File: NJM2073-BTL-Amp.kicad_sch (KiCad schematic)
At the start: 80 parts, among them J1 Screw_Terminal_01x02, J2 Screw_Terminal_01x02, J3 Barrel_Jack_Switch, J4 Conn_Coaxial_x2, J5 AudioJack3_SwitchTR, U3 NJM4558, U4 NJM4558

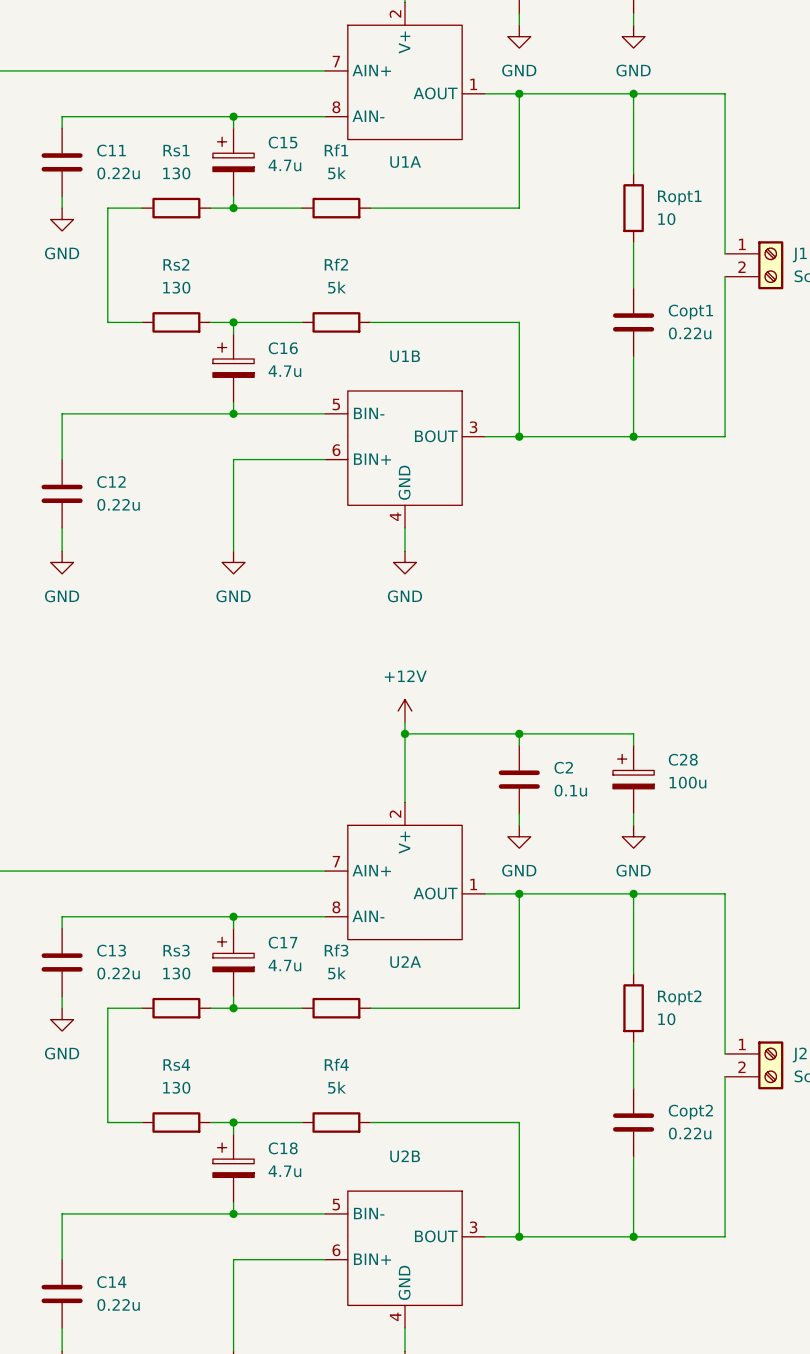
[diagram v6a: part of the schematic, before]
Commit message: シンボル名修正
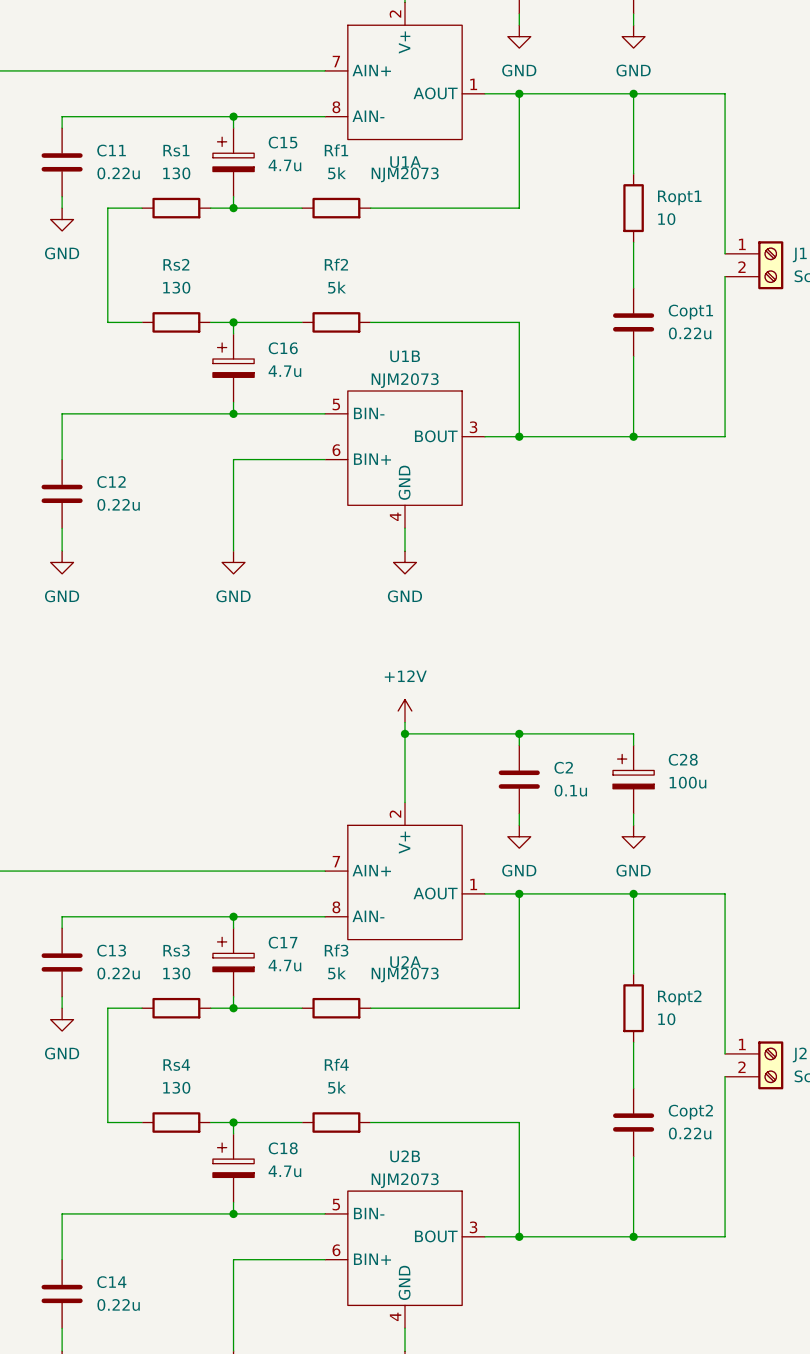
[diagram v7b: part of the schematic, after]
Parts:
- U1, U2: value ~ -> NJM2073
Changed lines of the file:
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@@
 			)
 		)
-		(property "Value" "~"
+		(property "Value" "NJM2073"
 			(at 342.9 148.59 0)
 			(effects
@@
 			)
 		)
-		(property "Value" "~"
+		(property "Value" "NJM2073"
 			(at 342.9 59.69 0)
 			(effects
@@
 			)
 		)
-		(property "Value" "~"
+		(property "Value" "NJM2073"
 			(at 342.9 171.45 0)
 			(effects
@@
 			)
 		)
-		(property "Value" "~"
+		(property "Value" "NJM2073"
 			(at 342.9 82.55 0)
 			(effects

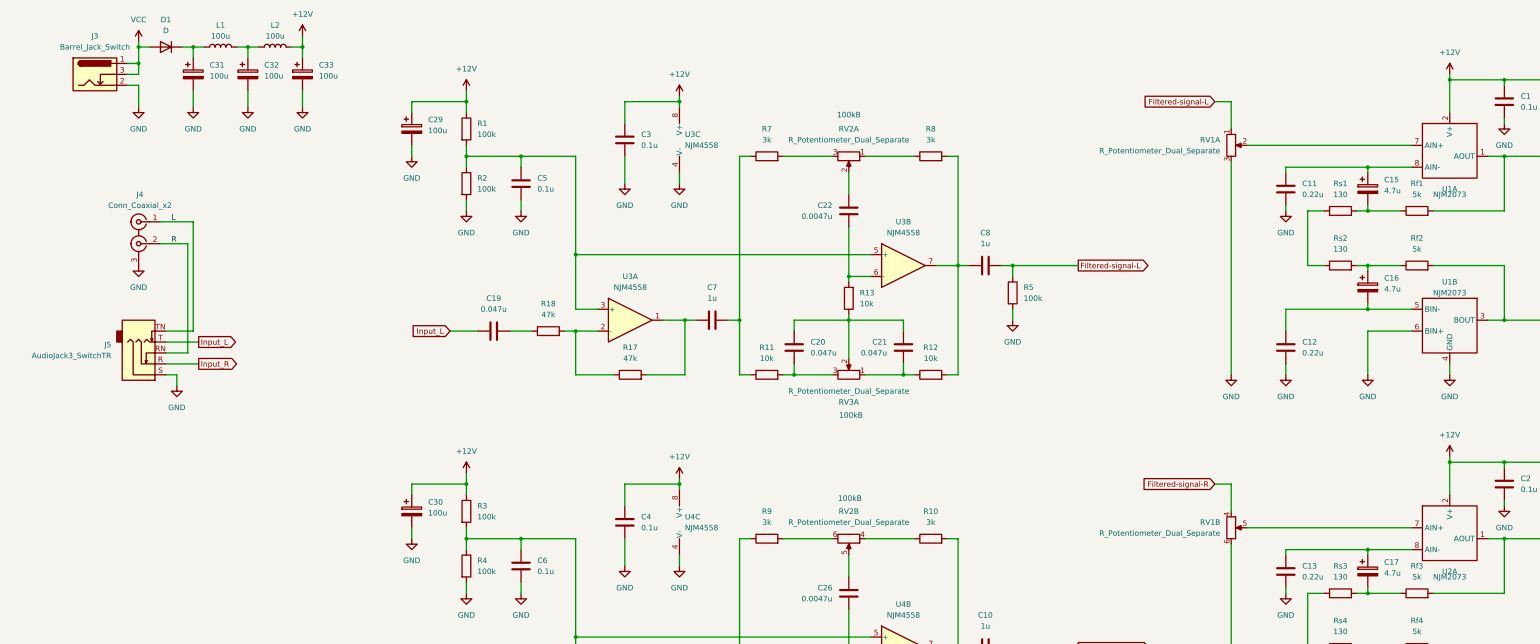
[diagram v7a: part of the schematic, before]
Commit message: 2073 の電源回路作成
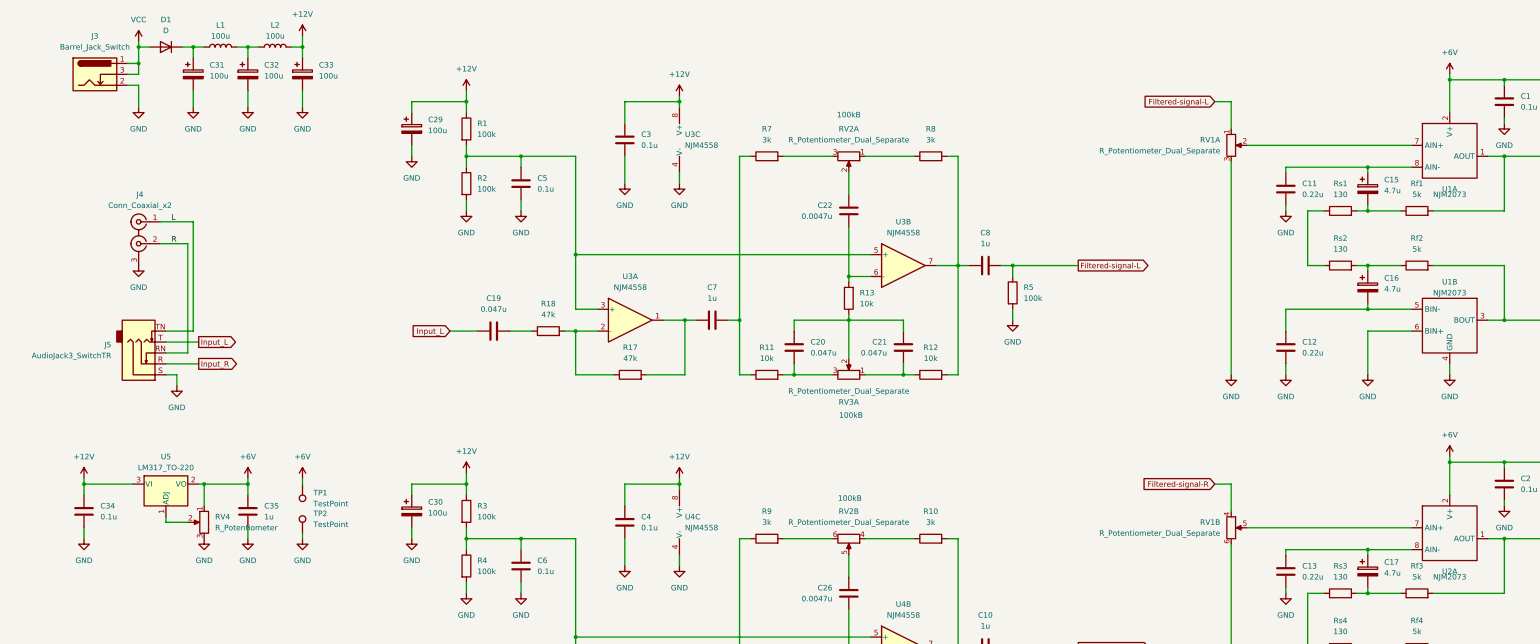
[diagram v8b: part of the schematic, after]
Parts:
- added C34: 0.1u, Capacitor_THT:C_Disc_D5.0mm_W2.5mm_P5.00mm, symbol Device:C
- added C35: 1u, Capacitor_THT:C_Disc_D5.0mm_W2.5mm_P5.00mm, symbol Device:C
- added RV4: R_Potentiometer, Potentiometer_THT:Potentiometer_ACP_CA9-H3,8_Horizontal, symbol Device:R_Potentiometer
- added TP1, TP2: TestPoint, TestPoint:TestPoint_Keystone_5000-5004_Miniature, symbol Connector:TestPoint
- added U5: LM317_TO-220, Package_TO_SOT_THT:TO-220-3_Vertical, symbol Regulator_Linear:LM317_TO-220
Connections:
- net +12V: now also C34.1, U5.3 (VI); no longer C1.1, C2.1, C27.1, C28.1, U1.2 (V+), U2.2 (V+)
- net GND: now also C34.2, C35.2, RV4.3, TP2.1
- new net: RV4.2, U5.1 (ADJ)
- new net +6V: C1.1, C2.1, C27.1, C28.1, C35.1, RV4.1, TP1.1, U1.2 (V+), U2.2 (V+), U5.2 (VO)
